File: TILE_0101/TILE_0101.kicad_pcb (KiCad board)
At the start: 2 copper layers, 42.1 x 24.6 mm, 3 parts

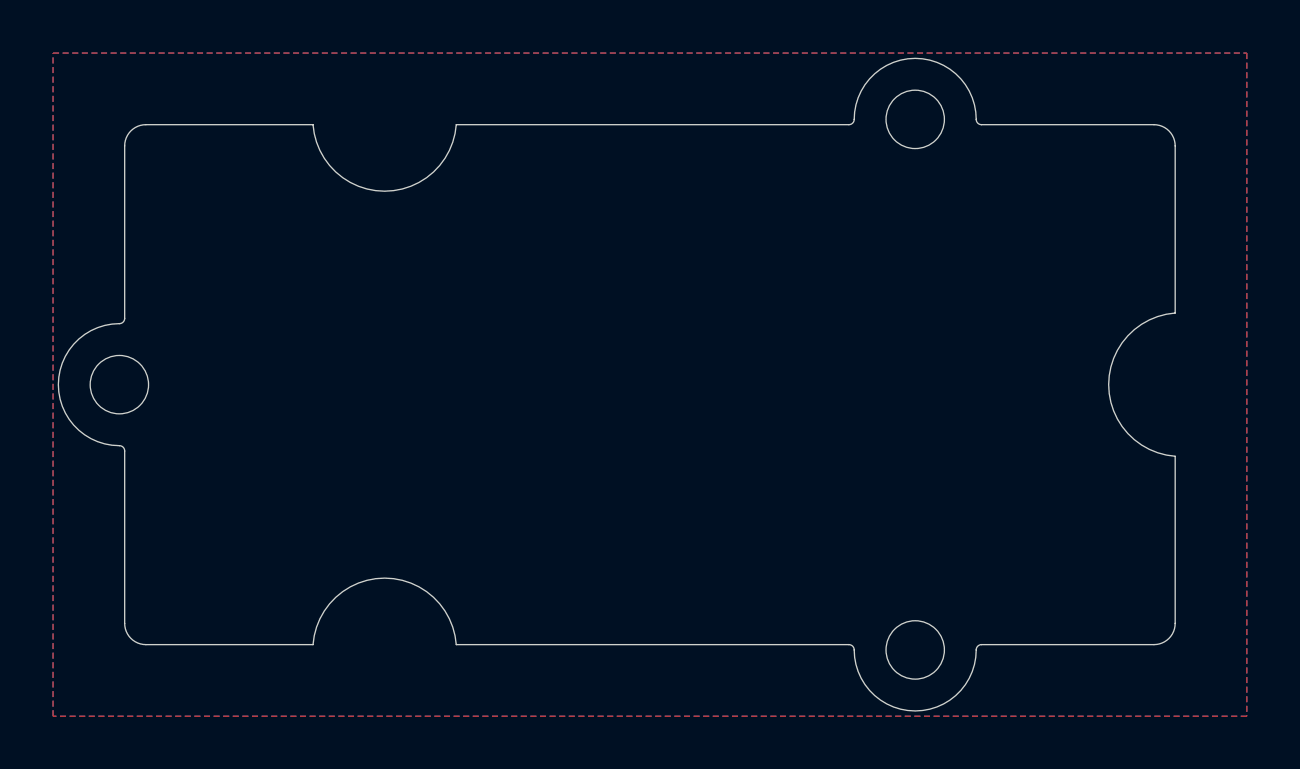
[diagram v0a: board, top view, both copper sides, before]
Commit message: Add 0101 and update images
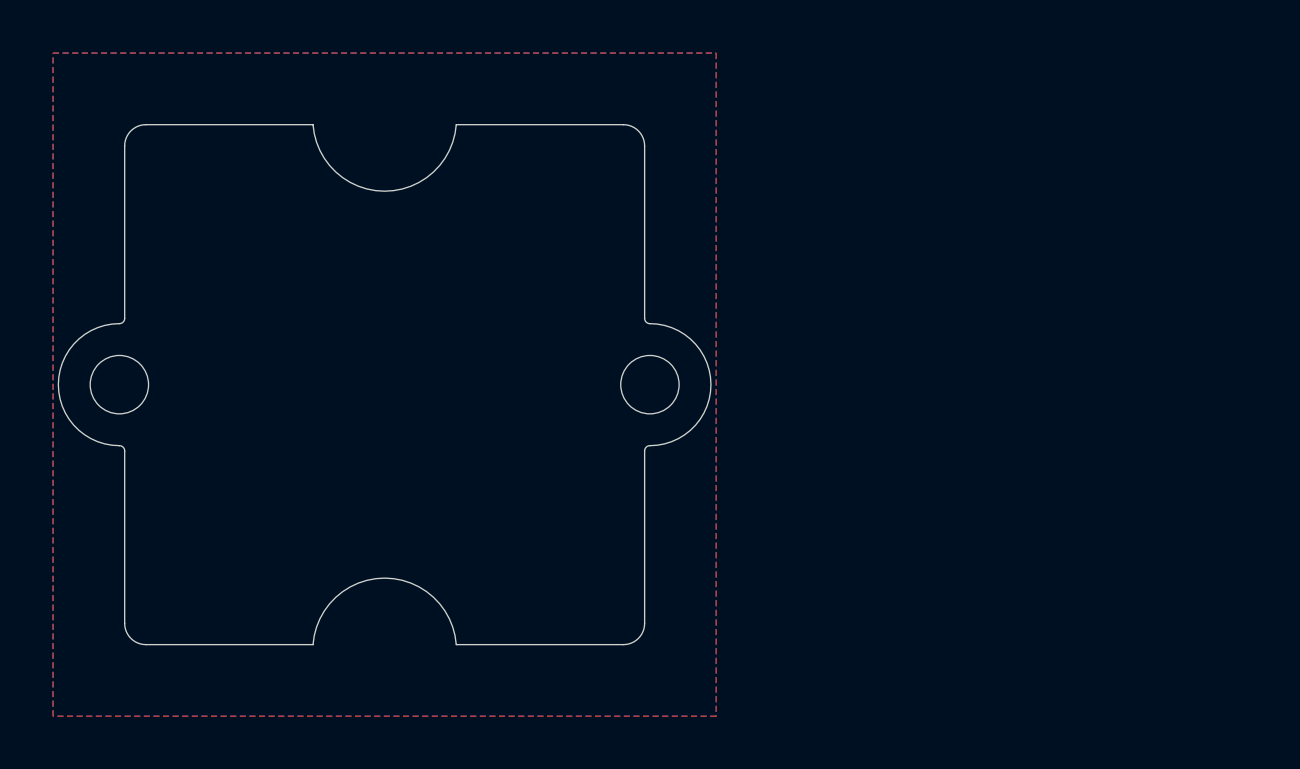
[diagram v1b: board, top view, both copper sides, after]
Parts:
- removed H3: MountingHole, MountingHole:MountingHole_2.2mm_M2
- moved H1 14.1 mm to (120.0, 110.0)
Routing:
- added copper zone on B.Cu, net (none)
- added copper zone on F.Cu, net (none)
- removed copper zone on B.Cu, net GND
- removed copper zone on F.Cu, net GND
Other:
- board size 42.1 x 24.6 mm -> 24.6 x 19.6 mm
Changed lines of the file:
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@@
   )
   (net 0 "")
-  (net 1 "GND")
   (footprint "MountingHole:MountingHole_2.2mm_M2" (layer "F.Cu")
-    (at 130 100)
+    (at 120 110)
     (descr "Mounting Hole 2.2mm, no annular, M2")
     (tags "mounting hole 2.2mm no annular m2")
-    (attr exclude_from_pos_files exclude_from_bom)
+    (property "Manufacturer" "~")
+    (property "PartNumber" "~")
+    (property "Sheetfile" "TILE_0101.kicad_sch")
+    (property "Sheetname" "")
+    (property "Supplier" "~")
+    (attr exclude_from_pos_files)
     (fp_text reference "H1" (at 0 -3.2) (layer "F.SilkS") hide
       (effects (font (size 1 1) (thickness 0.15)))
@@
     (descr "Mounting Hole 2.2mm, no annular, M2")
     (tags "mounting hole 2.2mm no annular m2")
-    (attr exclude_from_pos_files exclude_from_bom)
+    (property "Manufacturer" "~")
+    (property "PartNumber" "~")
+    (property "Sheetfile" "TILE_0101.kicad_sch")
+    (property "Sheetname" "")
+    (property "Supplier" "~")
+    (attr exclude_from_pos_files)
     (fp_text reference "H2" (at 0 -3.2) (layer "F.SilkS") hide
       (effects (font (size 1 1) (thickness 0.15)))
@@
     (pad "" np_thru_hole circle locked (at 0 0) (size 2.2 2.2) (drill 2.2) (layers *.Cu *.Mask))
   )
-  (footprint "MountingHole:MountingHole_2.2mm_M2" (layer "F.Cu")
-    (at 130 120)
-    (descr "Mounting Hole 2.2mm, no annular, M2")
-    (tags "mounting hole 2.2mm no annular m2")
-    (attr exclude_from_pos_files exclude_from_bom)
-    (fp_text reference "H3" (at 0 -3.2) (layer "F.SilkS") hide
-      (effects (font (size 1 1) (thickness 0.15)))
-    )
-    (fp_text value "MountingHole" (at 0 3.2) (layer "F.Fab")
-      (effects (font (size 1 1) (thickness 0.15)))
-    )
-    (fp_text user "${REFERENCE}" (at 0.3 0) (layer "F.Fab")
-      (effects (font (size 1 1) (thickness 0.15)))
-    )
-    (fp_circle (center 0 0) (end 2.2 0) (layer "Cmts.User") (width 0.15) (fill none))
-    (fp_circle (center 0 0) (end 2.45 0) (layer "F.CrtYd") (width 0.05) (fill none))
-    (pad "" np_thru_hole circle locked (at 0 0) (size 2.2 2.2) (drill 2.2) (layers *.Cu *.Mask))
-  )
-  (gr_line (start 140 100) (end 100 100) (layer "Dwgs.User") (width 0.05))
-  (gr_circle (center 130 120) (end 132.5 120) (layer "Dwgs.User") (width 0.05) (fill none))
-  (gr_circle (center 140 110) (end 142.5 110) (layer "Dwgs.User") (width 0.05) (fill none))
+  (gr_line (start 120 100) (end 100 100) (layer "Dwgs.User") (width 0.05))
+  (gr_circle (center 120 110) (end 122.5 110) (layer "Dwgs.User") (width 0.05) (fill none))
   (gr_circle (center 100 110) (end 102.5 110) (layer "Dwgs.User") (width 0.05) (fill none))
-  (gr_line (start 140 120) (end 140 100) (layer "Dwgs.User") (width 0.05))
+  (gr_line (start 120 120) (end 120 100) (layer "Dwgs.User") (width 0.05))
   (gr_circle (center 110 120) (end 112.5 120) (layer "Dwgs.User") (width 0.05) (fill none))
   (gr_line (start 100 100) (end 100 120) (layer "Dwgs.User") (width 0.05))
-  (gr_circle (center 130 100) (end 132.5 100) (layer "Dwgs.User") (width 0.05) (fill none))
   (gr_circle (center 110 100) (end 112.5 100) (layer "Dwgs.User") (width 0.05) (fill none))
-  (gr_line (start 100 120) (end 140 120) (layer "Dwgs.User") (width 0.05))
+  (gr_line (start 100 120) (end 120 120) (layer "Dwgs.User") (width 0.05))
   (gr_line (start 107.3 100.2) (end 101 100.2) (layer "Edge.Cuts") (width 0.05))
   (gr_line (start 100.2 112.5) (end 100.2 119) (layer "Edge.Cuts") (width 0.05))
-  (gr_line (start 132.5 100.2) (end 139 100.2) (layer "Edge.Cuts") (width 0.05))
   (gr_arc (start 107.3 119.8) (mid 110 117.292603) (end 112.7 119.8) (layer "Edge.Cuts") (width 0.05))
   (gr_arc (start 100 112.3) (mid 100.141421 112.358579) (end 100.2 112.5) (layer "Edge.Cuts") (width 0.05))
   (gr_arc (start 100.2 101) (mid 100.434315 100.434315) (end 101 100.2) (layer "Edge.Cuts") (width 0.05))
   (gr_arc (start 112.7 100.2) (mid 110 102.707397) (end 107.3 100.2) (layer "Edge.Cuts") (width 0.05))
-  (gr_line (start 112.7 100.2) (end 127.5 100.2) (layer "Edge.Cuts") (width 0.05))
-  (gr_arc (start 139.8 119) (mid 139.565685 119.565685) (end 139 119.8) (layer "Edge.Cuts") (width 0.05))
-  (gr_arc (start 132.5 100.2) (mid 132.358579 100.141421) (end 132.3 100) (layer "Edge.Cuts") (width 0.05))
-  (gr_line (start 139.8 119) (end 139.8 112.7) (layer "Edge.Cuts") (width 0.05))
-  (gr_line (start 139.8 101) (end 139.8 107.3) (layer "Edge.Cuts") (width 0.05))
-  (gr_arc (start 127.7 100) (mid 127.641421 100.141421) (end 127.5 100.2) (layer "Edge.Cuts") (width 0.05))
-  (gr_arc (start 139 100.2) (mid 139.565685 100.434315) (end 139.8 101) (layer "Edge.Cuts") (width 0.05))
-  (gr_arc (start 127.5 119.8) (mid 127.641421 119.858579) (end 127.7 120) (layer "Edge.Cuts") (width 0.05))
+  (gr_line (start 112.7 100.2) (end 119 100.2) (layer "Edge.Cuts") (width 0.05))
+  (gr_arc (start 119.8 119) (mid 119.565685 119.565685) (end 119 119.8) (layer "Edge.Cuts") (width 0.05))
+  (gr_arc (start 119.8 112.5) (mid 119.858579 112.358579) (end 120 112.3) (layer "Edge.Cuts") (width 0.05))
+  (gr_line (start 119.8 119) (end 119.8 112.5) (layer "Edge.Cuts") (width 0.05))
+  (gr_line (start 119.8 101) (end 119.8 107.5) (layer "Edge.Cuts") (width 0.05))
+  (gr_arc (start 120 107.7) (mid 119.858579 107.641421) (end 119.8 107.5) (layer "Edge.Cuts") (width 0.05))
+  (gr_arc (start 119 100.2) (mid 119.565685 100.434315) (end 119.8 101) (layer "Edge.Cuts") (width 0.05))
   (gr_arc (start 101 119.8) (mid 100.434315 119.565685) (end 100.2 119) (layer "Edge.Cuts") (width 0.05))
   (gr_line (start 101 119.8) (end 107.3 119.8) (layer "Edge.Cuts") (width 0.05))
   (gr_line (start 100.2 101) (end 100.2 107.5) (layer "Edge.Cuts") (width 0.05))
-  (gr_arc (start 127.7 100) (mid 130 97.7) (end 132.3 100) (layer "Edge.Cuts") (width 0.05))
+  (gr_arc (start 120 107.7) (mid 122.3 110) (end 120 112.3) (layer "Edge.Cuts") (width 0.05))
   (gr_arc (start 100 112.3) (mid 97.7 110) (end 100 107.7) (layer "Edge.Cuts") (width 0.05))
-  (gr_arc (start 139.799999 112.699999) (mid 137.292604 109.999999) (end 139.800001 107.300001) (layer "Edge.Cuts") (width 0.05))
-  (gr_arc (start 132.3 120) (mid 130 122.3) (end 127.7 120) (layer "Edge.Cuts") (width 0.05))
   (gr_arc (start 100.2 107.5) (mid 100.141421 107.641421) (end 100 107.7) (layer "Edge.Cuts") (width 0.05))
-  (gr_line (start 139 119.8) (end 132.5 119.8) (layer "Edge.Cuts") (width 0.05))
-  (gr_arc (start 132.3 120) (mid 132.358579 119.858579) (end 132.5 119.8) (layer "Edge.Cuts") (width 0.05))
-  (gr_line (start 127.5 119.8) (end 112.7 119.8) (layer "Edge.Cuts") (width 0.05))
+  (gr_line (start 119 119.8) (end 112.7 119.8) (layer "Edge.Cuts") (width 0.05))
   (dimension (type aligned) (layer "Dwgs.User")
-    (pts (xy 140 120) (xy 100 120))
+    (pts (xy 120 120) (xy 100 120))
     (height -5)
-    (gr_text "40.0000 mm" (at 120 123.85) (layer "Dwgs.User")
+    (gr_text "20.0000 mm" (at 110 123.85) (layer "Dwgs.User")
       (effects (font (size 1 1) (thickness 0.15)))
     )
@@
     (style (thickness 0.15) (arrow_length 1.27) (text_position_mode 0) (extension_height 0.58642) (extension_offset 0) keep_text_aligned)
   )
-  (zone (net 1) (net_name "GND") (layer "F.Cu") (hatch edge 0.508)
+  (zone (net 0) (net_name "") (layer "F.Cu") (hatch edge 0.508)
     (connect_pads (clearance 0.15))
     (min_thickness 0.254) (filled_areas_thickness no)
@@
     (polygon
       (pts
-        (xy 142.5 122.5)
+        (xy 122.5 122.5)
         (xy 97.5 122.5)
         (xy 97.5 97.5)
-        (xy 142.5 97.5)
+        (xy 122.5 97.5)
       )
     )
   )
-  (zone (net 1) (net_name "GND") (layer "B.Cu") (hatch edge 0.508)
+  (zone (net 0) (net_name "") (layer "B.Cu") (hatch edge 0.508)
     (connect_pads (clearance 0.15))
     (min_thickness 0.254) (filled_areas_thickness no)
@@
     (polygon
       (pts
-        (xy 142.5 122.5)
+        (xy 122.5 122.5)
         (xy 97.5 122.5)
         (xy 97.5 97.5)
-        (xy 142.5 97.5)
+        (xy 122.5 97.5)
       )
     )

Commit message: New design
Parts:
- removed H1, H2: MountingHole, MountingHole:MountingHole_2.2mm_M2
- added kibuzzard-63351A8A: G***, kibuzzard-63351A8A, F.Cu at (103.5, 101.5)
- added kibuzzard-63351A9D: G***, kibuzzard-63351A9D, F.Cu at (102.5, 118.5)
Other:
- board size 24.6 x 19.6 mm -> 19.6 x 19.6 mm
- board text added: "TEMPLATE"
